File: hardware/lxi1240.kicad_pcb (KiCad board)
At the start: 2 copper layers, 105.4 x 62.2 mm, 12 parts, among them J1 1240COMM, J2 1240COMM_EXT

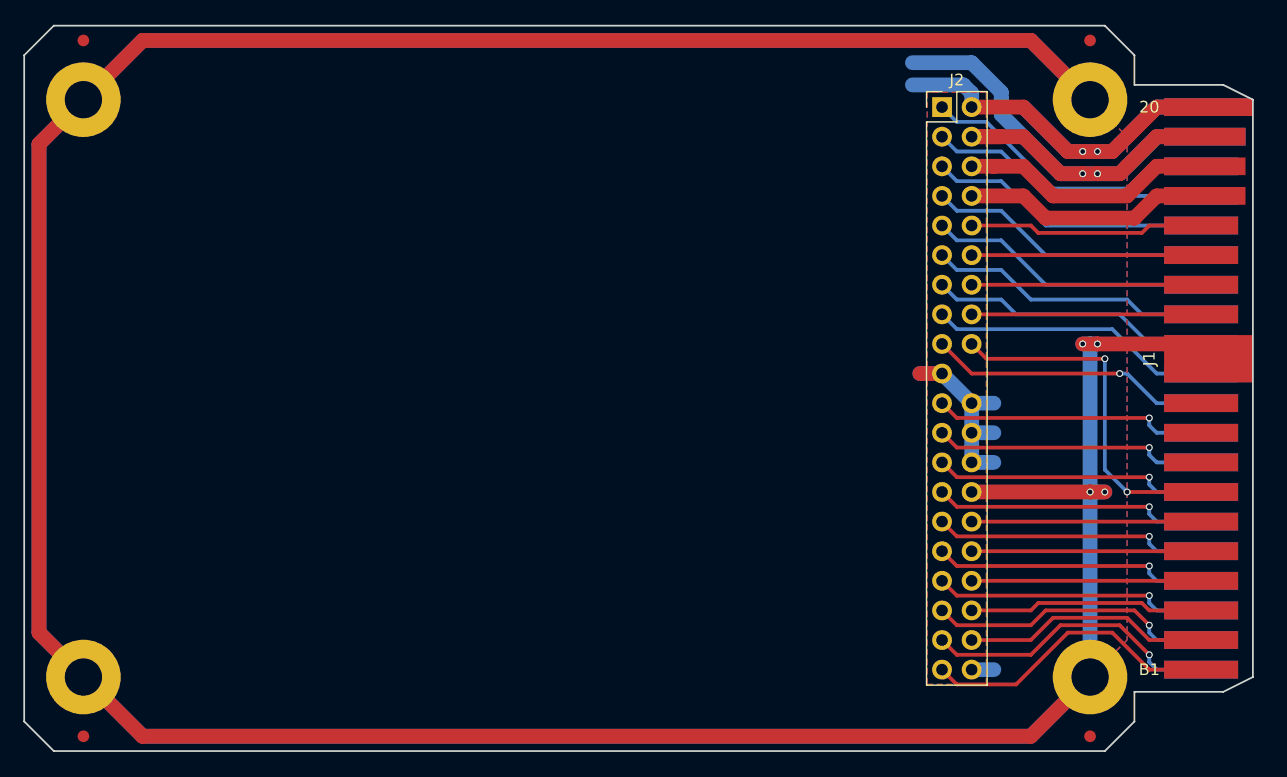
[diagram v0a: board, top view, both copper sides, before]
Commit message: Update board for more accurate measurements of the original.
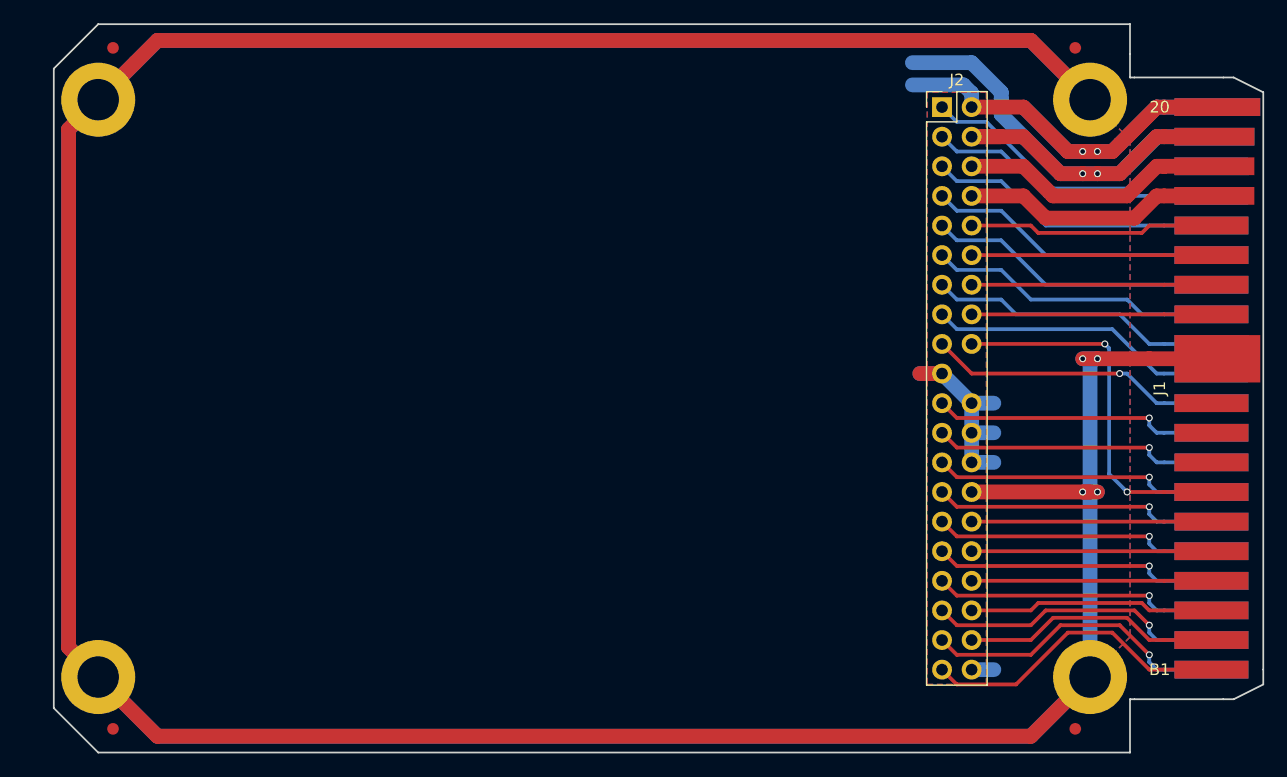
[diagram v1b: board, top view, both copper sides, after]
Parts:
- H1, H2, H3, H4: footprint Mounting_Holes:MountingHole_3.2mm_M3_Pad -> 1240comm:MountingHole_140mil_Pad
- J1: footprint 1240comm:1240COMM -> 1240COMM
- moved J1 26.8 mm to (214.2, 88.9)
- moved FD2 2.62 mm to (127.0, 118.1)
- moved FD3 2.62 mm to (127.0, 59.7)
- moved FD1 1.42 mm to (209.6, 118.1)
- moved FD4 1.42 mm to (209.6, 59.7)
- moved H2 1.27 mm to (125.7, 113.7)
- moved H3 1.27 mm to (125.7, 64.1)
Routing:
- net Earth_Protective: track 517.2 -> 510.2 mm
- net GND: track 65.2 -> 66.9 mm
- net +5V: track 53.2 -> 55.0 mm
- net /H-A13: track 27.4 -> 29.0 mm
- net /~H-RD: track 21.2 -> 22.4 mm
- net /H-A9: track 16.5 -> 17.8 mm
- net Net-(J1-PadA12): track 21.2 -> 22.0 mm
- net /~H-WR: track 22.6 -> 23.5 mm
- net /~H-RS: track 21.2 -> 22.0 mm
- net /~H-CS: track 17.0 -> 17.9 mm
- net /H-RST: track 21.5 -> 22.4 mm
- net /H-INT: track 21.2 -> 22.0 mm
- net /H-D7: track 20.5 -> 21.4 mm
- net /H-D6: track 20.5 -> 21.4 mm
- net /H-D5: track 20.5 -> 21.4 mm
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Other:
- board size 105.4 x 62.2 mm -> 103.8 x 62.5 mm

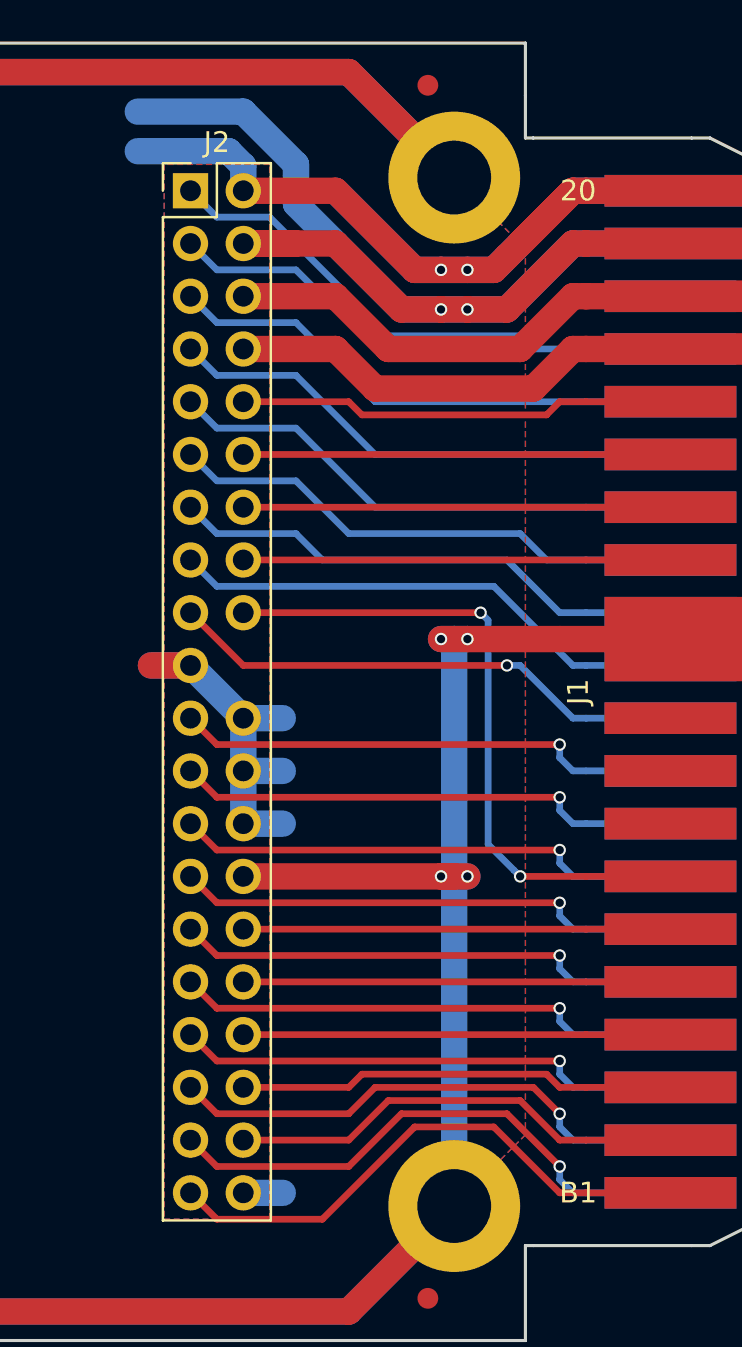
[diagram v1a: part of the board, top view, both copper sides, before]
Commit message: Move ATA header closer to board edge.
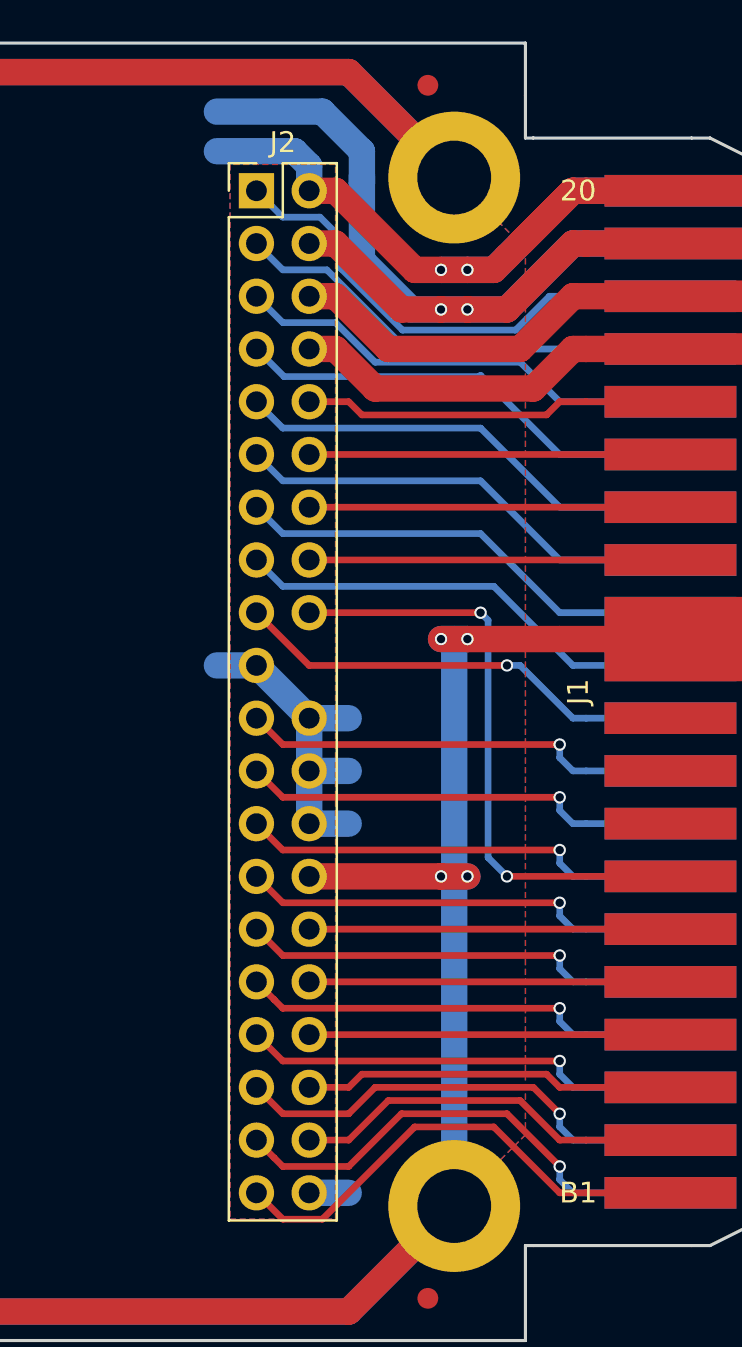
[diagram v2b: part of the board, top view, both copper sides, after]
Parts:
- moved J2 3.17 mm to (201.3, 64.8)
- moved Bonsai 1.27 mm to (184.2, 81.9)
- moved G*** 1.27 mm to (171.4, 81.3)
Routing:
- net GND: track 66.9 -> 54.6 mm
- net +5V: track 55.0 -> 47.8 mm
- net Earth_Protective: track 510.2 -> 506.4 mm
- net /H-A9: track 17.8 -> 14.2 mm
- net /~H-RD: track 22.4 -> 18.9 mm
- net /H-A6: track 17.9 -> 14.8 mm
- net /H-A8: track 17.4 -> 14.2 mm
- net /H-A7: track 17.4 -> 14.2 mm
- net /H-A3: track 19.0 -> 15.8 mm
- net /H-A12: track 17.4 -> 14.2 mm
- net /H-A11: track 17.4 -> 14.2 mm
- net /H-A10: track 17.4 -> 14.2 mm
- net -12VA: track 19.5 -> 16.3 mm
- net +12VA: track 19.0 -> 15.8 mm
- net /~H-CS: track 17.9 -> 14.8 mm
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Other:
- board text added: "G"
- board text added: "LXI Comm Pack for Tektronix 1240 v0.1 © 2017 Sam Hanes <sam@maltera.com> Licensed under CERN OHL v1.2 or newer https://github.com/Elemecca/lxi1240"
- board text added: "USE ATA RIBBON"
- board text removed: "LXI Comm Pack for Tektronix 1240 v0.1 © 2017 Sam Hanes <sam@maltera.com> Licensed under CERN OHL v1.2 or newer Software under GNU GPL v3 or newer https://github.com/Elemecca/lxi1240"
- board text removed: "SOCKET EXTENDER USE 80-CONDUCTOR ATA RIBBON"
